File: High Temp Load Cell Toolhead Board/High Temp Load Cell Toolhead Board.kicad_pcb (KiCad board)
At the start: 4 copper layers, 60 x 60 mm, 118 parts, among them J1 Conn_01x03, J11 Conn_01x03, J12 Conn_01x03, J13 PinHeader_2x4_P2.54mm, J2 Conn_02x08, J6 Conn_01x04, J7 Conn_01x02, J8 Conn_01x04, J9 Conn_01x02, P1 USB_C_Plug_USB2.0, Q1 DMG3404L, Q2 DMG3404L, SW1 SW_SPST, U1 MAX31865xTP, U2 STM32F103CBU6TR, U3 SN74LVC2G17DSFR, U4 SN74AHC1G32QDBVRQ1, U5 ADS1220, X1 ECS-2520MVLC-080-BP-TR

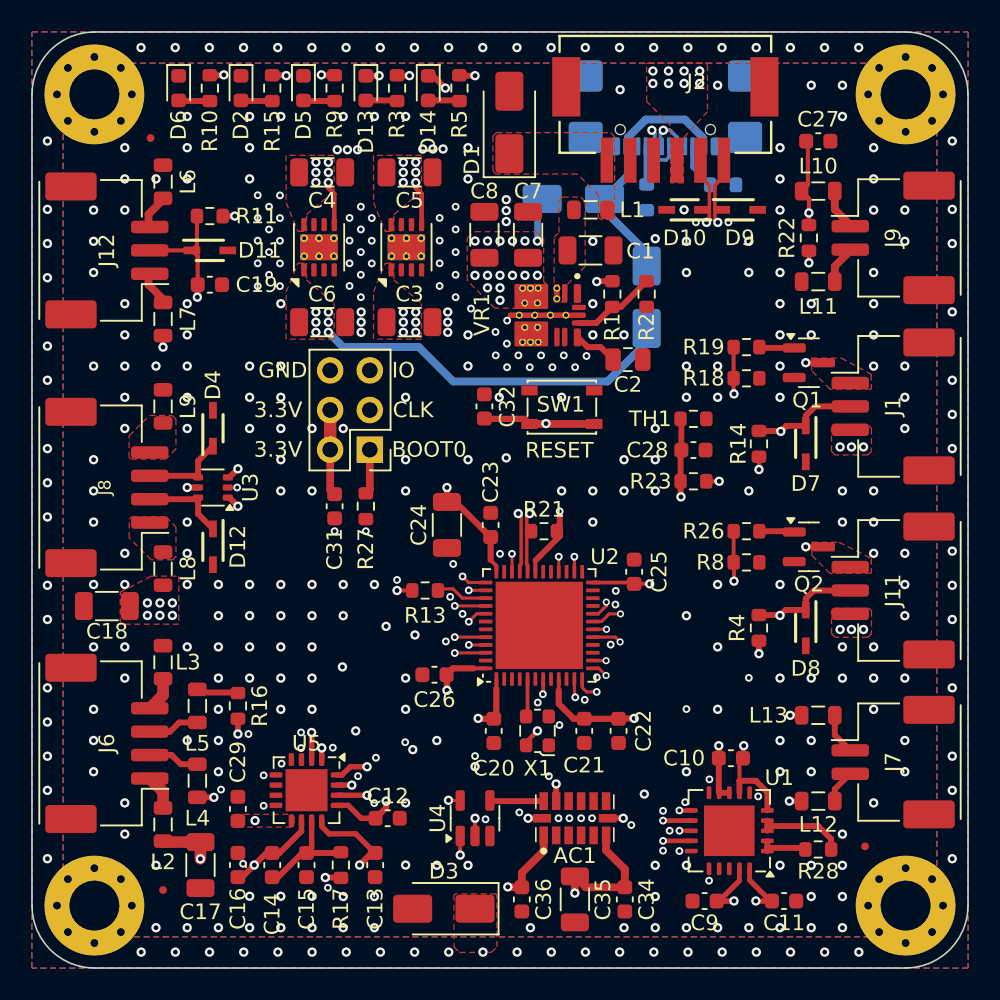
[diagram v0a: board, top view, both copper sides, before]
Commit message: Replace Oscillator Module with Crystal
* After a bunch of research I've concluded that I cant use the Oscillator Module with Katapult's codebase for the STM32 chips. Added discussion on this to the design doc. Updated design to use a crystal and 2 caps. Exact capacitor values to be calculated later

* Based on the best advice I can find for decoupling capacitors on the MCU I have moved them to the back side of the board. This allows their footprints to overlap with the MCU itself, reducing the distance from the MCU to the decoupling cap. Also added vias next to the 2 pins  on the MCU that are true ground pins. There are other ground connections through GPIO pins but these are high impedance.

* Removed the power planes on layer 3 and replaced them with traces. With the additional components on the bottom layer, its more advantageous to have layer 3 be a ground reference for layer 4 in the places where items are routed on that layer. Power planes were easier to maintain but I don't think this board has any power delivery problems.

* Removed the extra diode and routing from the USB supply. Its not a requirement that the 5V rail power up from USB.
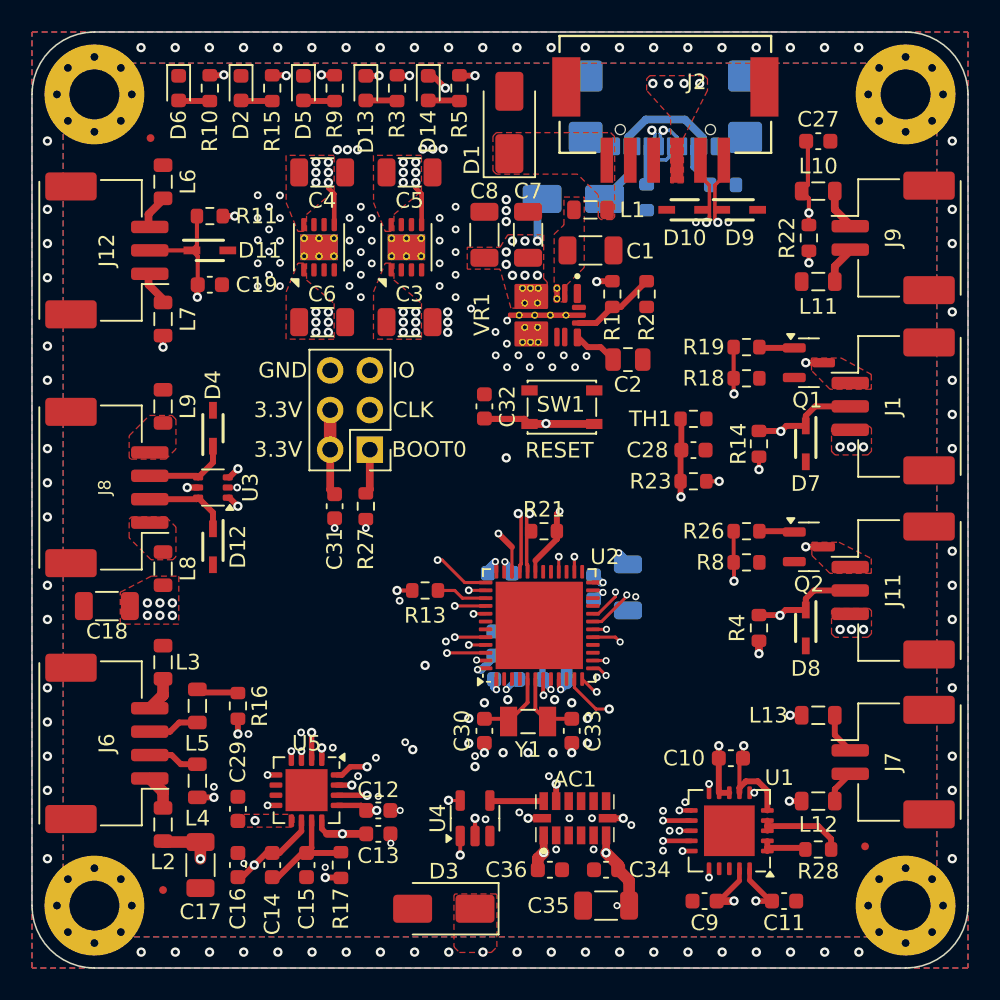
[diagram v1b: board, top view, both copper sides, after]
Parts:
- removed D16: 40V, 1A, SMA, Diode_SMD:D_SMA
- removed X1: ECS-2520MVLC-080-BP-TR, Oscillator:Oscillator_SMD_ECS_2520MV-xxx-xx-4Pin_2.5x2.0mm
- added C30: 2?pF, Capacitor_SMD:C_0603_1608Metric, F.Cu at (29.0, 44.8)
- added C33: 2?pF, Capacitor_SMD:C_0603_1608Metric, F.Cu at (34.6, 44.8)
- added Y1: Crystal ECS-.327-6-34QCS-TR, ECS-.327-6-34QCS-TR:XTAL_ECS-.327-6-34QCS-TR, F.Cu at (31.8, 44.2)
- C20, C21, C22, C23, C24, C25, C26: moved to B.Cu
- moved C24 12.3 mm to (38.2, 35.6)
- moved C21 11.5 mm to (30.0, 34.7), turned to 180 degrees
- moved C23 9.26 mm to (33.5, 39.9), turned to 0 degrees
- moved C22 7.92 mm to (30.4, 41.5), turned to 180 degrees
- moved C20 5.11 mm to (33.5, 41.5), turned to 0 degrees
- moved C26 4.29 mm to (29.6, 39.2), turned to -90 degrees
- moved C25 2.79 mm to (36.0, 35.6), turned to 90 degrees
- moved C36 2.62 mm to (33.2, 53.7), turned to 0 degrees
- moved C34 2.25 mm to (36.8, 53.7), turned to 180 degrees
- moved C35 2.04 mm to (36.8, 56.0), turned to 180 degrees
- moved C13 2.01 mm to (22.2, 51.4), turned to 180 degrees
- moved C12 0.78 mm to (22.2, 49.9)
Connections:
- net Net-(AC1-SDA/SDI/SDIO) renamed /SPI_1_SDO_OR_CS
- net Net-(D15-A) renamed /+5V_USB
- U2 pad 10: unconnected-(U2-PA0-Pad10) -> GND
- U2 pad 15: unconnected-(U2-PA5-Pad15) -> GND
- U2 pad 16: unconnected-(U2-PA6-Pad16) -> GND
- U2 pad 2: unconnected-(U2-PC13-Pad2) -> GND
- U2 pad 21: unconnected-(U2-PB10-Pad21) -> GND
- U2 pad 22: unconnected-(U2-PB11-Pad22) -> GND
- U2 pad 25: unconnected-(U2-PB12-Pad25) -> GND
- U2 pad 27: unconnected-(U2-PB14-Pad27) -> GND
- U2 pad 29: unconnected-(U2-PA8-Pad29) -> GND
- U2 pad 3: unconnected-(U2-PC14-Pad3) -> GND
- U2 pad 30: unconnected-(U2-PA9-Pad30) -> GND
- U2 pad 4: unconnected-(U2-PC15-Pad4) -> GND
- U2 pad 42: unconnected-(U2-PB6-Pad42) -> GND
- U2 pad 43: unconnected-(U2-PB7-Pad43) -> GND
- U2 pad 5: Net-(U2-PD0) -> /OSC_IN
- U2 pad 6: unconnected-(U2-PD1-Pad6) -> /OSC_OUT
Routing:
- net +3V3: track 63.0 -> 250.0 mm, vias 25 -> 26
- net /+FANV_INPUT: track 17.8 -> 67.9 mm, vias 16 -> 12
- net +5V: track 51.3 -> 93.2 mm
- net +5V5: track 13.6 -> 30.8 mm, vias 28 -> 21
- net /+5V_USB: track 16.3 -> 10.9 mm
- net GND: track 0.00 -> 5.24 mm, vias 331 -> 121
- net /OSC_IN: track 0.00 -> 4.85 mm
- net /OSC_OUT: track 0.00 -> 4.67 mm
- net FILAMENT_SW: track 42.3 -> 45.7 mm
- net Net-(U2-PD0): track 2.43 -> 0.00 mm
- net FAN1_TACH: track 20.7 -> 22.3 mm
- net SWD_IO: track 18.1 -> 16.7 mm
- added copper zone on In1.Cu, net +5V5
- removed copper zone on In2.Cu, net +5V
- removed copper zone on In2.Cu, net +5V5
- removed copper zone on In2.Cu, net /+FANV_INPUT

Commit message: Add Via Stitching
* Re-run via stitching on GND
* Add capacitor values to crystal caps
* Update design doc
* Remove bad assembly document
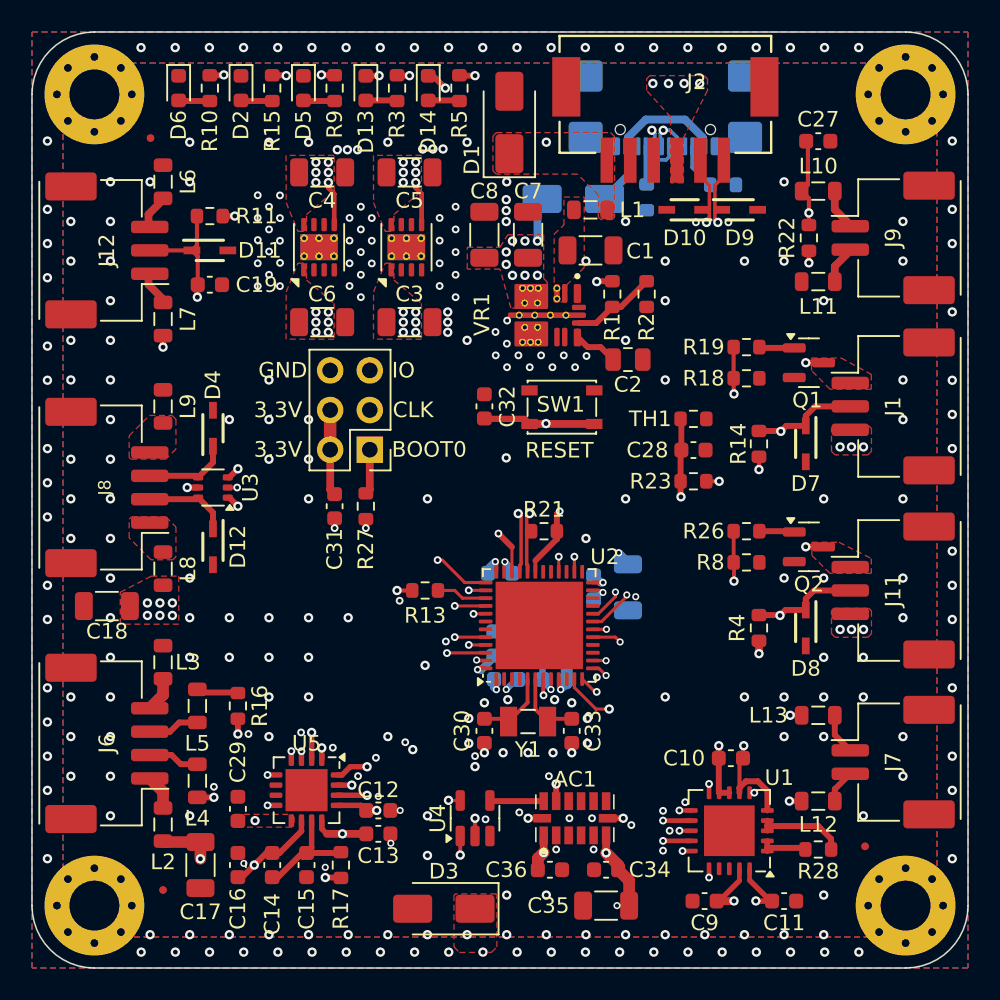
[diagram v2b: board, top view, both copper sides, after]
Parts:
- C30, C33: value 2?pF -> 25pF
- Y1: value Crystal ECS-.327-6-34QCS-TR -> Crystal
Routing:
- net +5V5: track 30.8 -> 29.2 mm
- net GND: vias 121 -> 237

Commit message: WIP Address community comments
* Switch to 6 layers and update design rules for new 6 layer process
* Change fan MOSFETs based on feedback. Drive MOSFETs with level shifter at 5V
* Add a 5V LDO for the loadcell thats not potentially poisoned by 5V LED noise
* Delete MAX chip, switch to PT1000
* Use 2 SPI busses, delete CS lines
* Move all components to front of board, re-organize layout to fit everything
* Switch to vertical USBC connector and import model

The schematic is updated but the routing has not been done
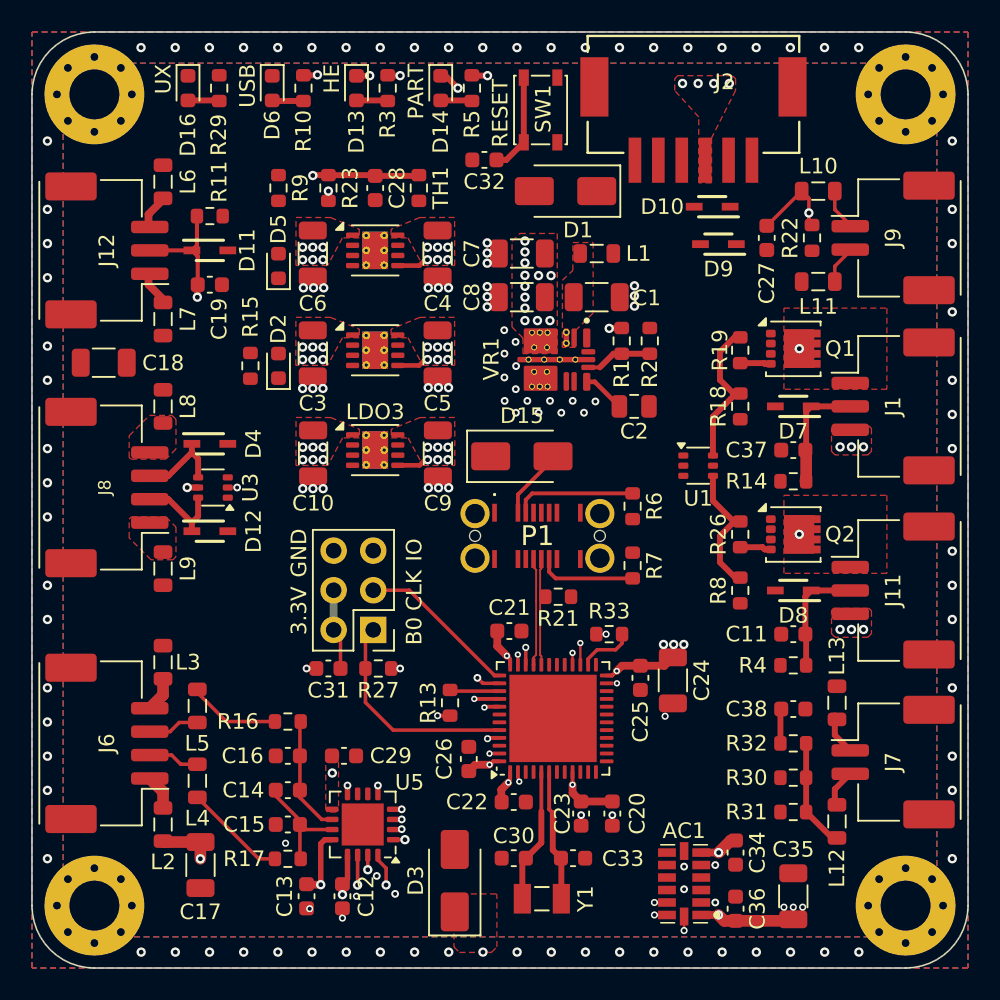
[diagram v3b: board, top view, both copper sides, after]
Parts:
- removed FID1, FID2, FID3: Fiducial, Fiducial:Fiducial_0.5mm_Mask1.5mm
- removed R28: R430Ω, Resistor_SMD:R_0603_1608Metric
- removed U4: SN74AHC1G32QDBVRQ1, Package_TO_SOT_SMD:SOT-23-5
- added C37: 0.1uF, Capacitor_SMD:C_0603_1608Metric, F.Cu at (48.8, 26.8)
- added C38: 0.1uF, Capacitor_SMD:C_0603_1608Metric, F.Cu at (48.8, 43.4)
- added D16: RED LED, LED_SMD:LED_0603_1608Metric, F.Cu at (10.0, 3.60)
- added LDO3: TPS7A21-Q1 5V @ 500mA, Package_SON:VSON-8-1EP_3x3mm_P0.65mm_EP1.65x2.4mm_ThermalVias, F.Cu at (22.0, 26.8)
- added R29: R1kΩ, Resistor_SMD:R_0603_1608Metric, F.Cu at (12.0, 3.60)
- added R30: R4.7kΩ, Resistor_SMD:R_0603_1608Metric, F.Cu at (48.8, 47.8)
- added R31: R2.2kΩ, Resistor_SMD:R_0603_1608Metric, F.Cu at (48.8, 50.0)
- added R32: R4.7kΩ, Resistor_SMD:R_0603_1608Metric, F.Cu at (48.8, 45.6)
- added R33: R47Ω, Resistor_SMD:R_0603_1608Metric, F.Cu at (37.0, 38.6)
- C10, C9: value 0.1uF -> 10uF; footprint Capacitor_SMD:C_0603_1608Metric -> Capacitor_SMD:C_1206_3216Metric
- C20, C21, C22, C23, C24, C25, C26, D15, R6, R7: moved to F.Cu
- LDO1: value TPS7121-Q1 5V @ 500mA -> TPS7A21-Q1 5V @ 500mA
- LDO2: value TPS7121-Q1 3.3V @ 500mA -> TPS7A21-Q1 3.3V @ 500mA
- P1: footprint Connector_USB:USB_C_Receptacle_GCT_USB4110 -> GCT_USB4145-03-0170-C:USB4145030170C; moved to F.Cu
- Q1, Q2: value DMG3404L -> CSD17581Q3A; footprint Package_TO_SOT_SMD:SOT-23 -> Package_SON:VSON-8_3.3x3.3mm_P0.65mm_NexFET
- U1: value MAX31865xTP -> SN74LVC2G17DSFR; footprint Package_DFN_QFN:TQFN-20-1EP_5x5mm_P0.65mm_EP3.25x3.25mm -> Package_TO_SOT_SMD:SOT-363_SC-70-6
- moved C9 33.4 mm to (26.0, 27.0), turned to -90 degrees
- moved C10 33.2 mm to (18.0, 27.0), turned to -90 degrees
- moved R23 30.0 mm to (19.0, 10.0), turned to -90 degrees
- moved P1 29.8 mm to (32.4, 32.3)
- moved C28 26.4 mm to (22.0, 10.0), turned to -90 degrees
- moved R7 25.1 mm to (38.5, 34.2), turned to 90 degrees
- moved U1 23.5 mm to (42.7, 27.8), turned to 0 degrees
- moved TH1 23.0 mm to (24.8, 10.0), turned to -90 degrees
- moved R6 19.8 mm to (38.5, 30.4)
- moved SW1 19.1 mm to (32.6, 5.00), turned to 90 degrees
- moved D2 18.0 mm to (15.8, 21.4), turned to 90 degrees
- moved R15 17.9 mm to (14.0, 21.4)
- moved C11 17.1 mm to (48.8, 38.6), turned to 180 degrees
- moved D15 16.8 mm to (31.4, 27.2)
- moved C32 15.8 mm to (29.0, 8.20), turned to 180 degrees
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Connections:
- net /PT100+ renamed /PT1000+
- net /PT100- renamed /PT1000-
- AC1 pad 12: SPI_1_SDI -> SPI_2_SDI
- AC1 pad 13: /SPI_1_SDO_OR_CS -> SPI_2_SDO
- AC1 pad 14: SPI_1_SCLK -> SPI_2_SCLK
- AC1 pad 7: ADXL345_CS -> GND
- C10 pad 1: Net-(U1-FORCE+) -> +5VA
- C10 pad 2: Net-(U1-FORCE-) -> GND
- C11 pad 1: +3V3 -> FAN1_TACH
- C13 pad 2: +5V -> +5VA
- C17 pad 1: +5V -> +5VA
- C29 pad 1: +5V -> +5VA
- C9 pad 1: +3V3 -> +5V5
- J8 pad 1: /LED_POWER -> /LED_GND
- J8 pad 4: /LED_GND -> /LED_POWER
- L12 pad 1: Net-(U1-FORCE+) -> Net-(L12-Pad1)
- L13 pad 2: Net-(U1-FORCE-) -> GND
- L2 pad 2: +5V -> +5VA
- Q1 pad 1: Net-(Q1-G) -> GND
- Q1 pad 3: /FAN0_MOSFET_GND -> GND
- Q2 pad 1: Net-(Q2-G) -> GND
- Q2 pad 3: /FAN1_MOSFET_GND -> GND
- R18 pad 2: FAN0_PWM -> /FAN0_PWM_+5V
- R19 pad 2: FAN0_PWM -> /FAN0_PWM_+5V
- R26 pad 2: FAN1_PWM -> /FAN1_PWM_+5V
- R8 pad 2: FAN1_PWM -> /FAN1_PWM_+5V
- U1 pad 1: Net-(U1-BIAS) -> FAN0_PWM
- U1 pad 2: Net-(U1-BIAS) -> GND
- U1 pad 3: Net-(U1-ISENSOR) -> FAN1_PWM
- U1 pad 4: Net-(U1-ISENSOR) -> /FAN1_PWM_+5V
- U1 pad 5: Net-(U1-FORCE+) -> +5V
- U1 pad 6: GND -> /FAN0_PWM_+5V
- U2 pad 11: ADXL345_CS -> GND
- U2 pad 12: MAX31865_CS -> PT1000
- U2 pad 26: LED_MCU_SDO -> Net-(U2-PB13)
- U2 pad 27: GND -> SPI_2_SDI
- U2 pad 28: LED_MCU_CLK -> SPI_2_SDO
- U2 pad 29: GND -> INDICATOR_LED
- U2 pad 42: GND -> LED_MCU_SDO
- U2 pad 43: GND -> LED_MCU_CLK
- U2 pad 46: ADS1220_CS -> GND
- U5 pad 12: +5V -> +5VA
- U5 pad 2: ADS1220_CS -> GND
- U5 pad 9: +5V -> +5VA
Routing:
- net +3V3: track 250.0 -> 32.8 mm, vias 26 -> 21
- net +5V: track 93.2 -> 0.70 mm, vias 17 -> 7
- net USB_PULL_UP: track 46.7 -> 0.88 mm, vias 3 -> 1
- net USB_D-: track 44.6 -> 6.93 mm, vias 3 -> 0
- net USB_D+: track 43.8 -> 6.84 mm, vias 3 -> 0
- net SPI_1_SCLK: track 43.1 -> 10.2 mm, vias 4 -> 2
- net HEATBREAK_THERMISTOR: track 38.8 -> 6.30 mm, vias 2 -> 1
- net LED_MCU_SDO: track 28.7 -> 0.00 mm, vias 2 -> 0
- net LED_MCU_CLK: track 27.4 -> 0.00 mm, vias 2 -> 0
- net SPI_1_SDO: track 42.7 -> 17.1 mm, vias 5 -> 2
- net SPI_1_SDI: track 43.3 -> 18.1 mm, vias 4 -> 2
- net NRST: track 30.8 -> 6.37 mm, vias 2 -> 0
- net ADXL345_CS: track 24.4 -> 0.00 mm, vias 3 -> 0
- net SPI_2_SCLK: track 0.00 -> 23.6 mm, vias 0 -> 2
- net FAN0_PWM: track 23.1 -> 0.00 mm, vias 2 -> 0
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- added copper zone on In2.Cu, net +5V5
- added copper zone on F.Cu, net +5VA
- added copper zone on In3.Cu, net GND
- added copper zone on In4.Cu, net GND
- removed copper zone on In1.Cu, net +5V5
- removed copper zone on F.Cu, net /+24V_INPUT
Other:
- copper layers 4 -> 6
- board text added: "B0"
- board text added: "HE"
- board text added: "PART"
- board text added: "USB"
- board text added: "UX"
- board text removed: "BOOT0"
